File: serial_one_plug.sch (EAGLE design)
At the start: 3 parts

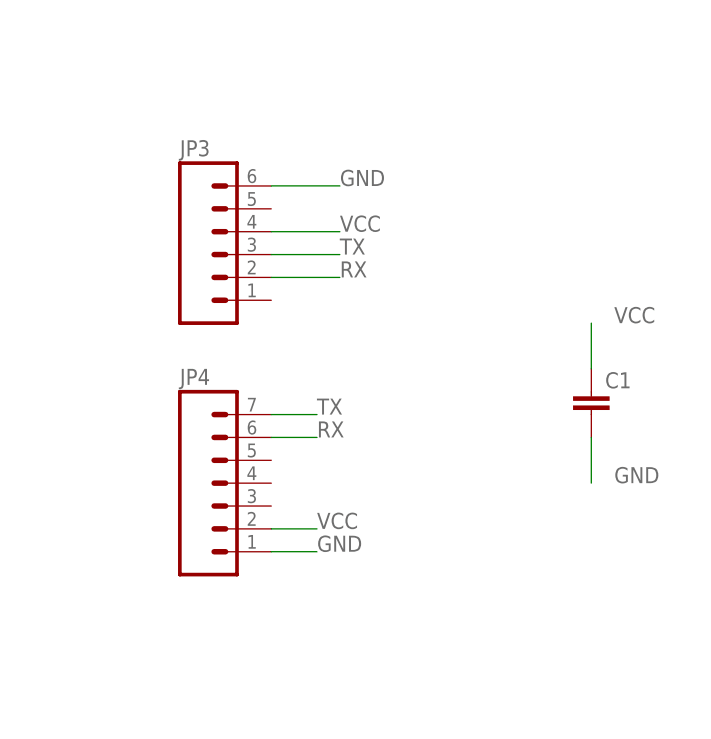
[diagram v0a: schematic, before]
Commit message: serial plug version 2 -- reset + prog
added more (more more!) functionality to the serial plug
has a ground jumper for PD2, pushbutton on reset
enabling it to work with bootloader
printed out, run, it's great.
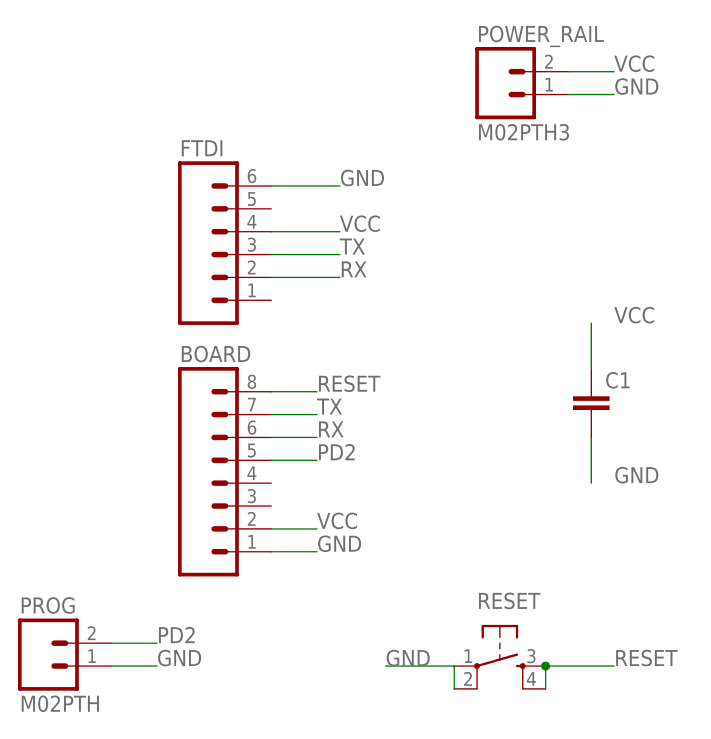
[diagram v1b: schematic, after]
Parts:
- removed JP4: (no value), SparkFun-Connectors:M07LONGPADS
- added BOARD: (no value), SparkFun-Connectors:M08LONGPADS
- added POWER_RAIL: M02PTH3, SparkFun-Connectors:M02PTH3
- added PROG: M02PTH, SparkFun-Connectors:M02PTH
- added RESET: (no value), SparkFun-Electromechanical:TAC_SWITCHPTH
- renumbered JP3 to FTDI
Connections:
- new net PD2: BOARD.5, PROG.2
- new net RESET: BOARD.8, RESET.3, RESET.4
- net GND: now also BOARD.1, POWER_RAIL.1, PROG.1, RESET.1, RESET.2; no longer JP4.1
- net RX: now also BOARD.6; no longer JP4.6
- net TX: now also BOARD.7; no longer JP4.7
- net VCC: now also BOARD.2, POWER_RAIL.2; no longer JP4.2
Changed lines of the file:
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@@
 <parts>
 <part name="C1" library="resistor" deviceset="C-EU" device="C1210"/>
-<part name="JP3" library="SparkFun-Connectors" deviceset="M06" device="LONGPADS"/>
-<part name="JP4" library="SparkFun-Connectors" deviceset="M07" device="LONGPADS"/>
+<part name="FTDI" library="SparkFun-Connectors" deviceset="M06" device="LONGPADS"/>
+<part name="POWER_RAIL" library="SparkFun-Connectors" deviceset="M02" device="PTH3"/>
+<part name="BOARD" library="SparkFun-Connectors" deviceset="M08" device="LONGPADS"/>
+<part name="RESET" library="SparkFun-Electromechanical" deviceset="TAC_SWITCH" device="PTH"/>
+<part name="PROG" library="SparkFun-Connectors" deviceset="M02" device="PTH"/>
 </parts>
 <sheets>
@@
 <instances>
 <instance part="C1" gate="G$1" x="33.02" y="0"/>
-<instance part="JP3" gate="G$1" x="-7.62" y="15.24"/>
-<instance part="JP4" gate="G$1" x="-7.62" y="-12.7"/>
+<instance part="FTDI" gate="G$1" x="-7.62" y="15.24"/>
+<instance part="POWER_RAIL" gate="G$1" x="22.86" y="33.02"/>
+<instance part="BOARD" gate="G$1" x="-7.62" y="-10.16"/>
+<instance part="RESET" gate="S" x="22.86" y="-30.48"/>
+<instance part="PROG" gate="G$1" x="-27.94" y="-30.48"/>
 </instances>
 <busses>
@@
 <wire x1="-2.54" y1="22.86" x2="5.08" y2="22.86" width="0.1524" layer="91"/>
 <label x="5.08" y="22.86" size="1.778" layer="95"/>
-<pinref part="JP3" gate="G$1" pin="6"/>
+<pinref part="FTDI" gate="G$1" pin="6"/>
 </segment>
 <segment>
 <wire x1="-2.54" y1="-17.78" x2="2.54" y2="-17.78" width="0.1524" layer="91"/>
 <label x="2.54" y="-17.78" size="1.778" layer="95"/>
-<pinref part="JP4" gate="G$1" pin="1"/>
+<pinref part="BOARD" gate="G$1" pin="1"/>
 </segment>
 <segment>
@@
 <label x="35.56" y="-10.16" size="1.778" layer="95"/>
 </segment>
+<segment>
+<pinref part="POWER_RAIL" gate="G$1" pin="1"/>
+<wire x1="30.48" y1="33.02" x2="35.56" y2="33.02" width="0.1524" layer="91"/>
+<label x="35.56" y="33.02" size="1.778" layer="95"/>
+</segment>
+<segment>
+<pinref part="RESET" gate="S" pin="1"/>
+<pinref part="RESET" gate="S" pin="2"/>
+<wire x1="10.16" y1="-30.48" x2="17.78" y2="-30.48" width="0.1524" layer="91"/>
+<wire x1="17.78" y1="-30.48" x2="17.78" y2="-33.02" width="0.1524" layer="91"/>
+<label x="10.16" y="-30.48" size="1.778" layer="95"/>
+</segment>
+<segment>
+<pinref part="PROG" gate="G$1" pin="1"/>
+<wire x1="-20.32" y1="-30.48" x2="-15.24" y2="-30.48" width="0.1524" layer="91"/>
+<label x="-15.24" y="-30.48" size="1.778" layer="95"/>
+</segment>
 </net>
 <net name="VCC" class="0">
@@
 <wire x1="-2.54" y1="17.78" x2="5.08" y2="17.78" width="0.1524" layer="91"/>
 <label x="5.08" y="17.78" size="1.778" layer="95"/>
-<pinref part="JP3" gate="G$1" pin="4"/>
+<pinref part="FTDI" gate="G$1" pin="4"/>
 </segment>
 <segment>
 <wire x1="-2.54" y1="-15.24" x2="2.54" y2="-15.24" width="0.1524" layer="91"/>
 <label x="2.54" y="-15.24" size="1.778" layer="95"/>
-<pinref part="JP4" gate="G$1" pin="2"/>
+<pinref part="BOARD" gate="G$1" pin="2"/>
 </segment>
 <segment>
@@
 <label x="35.56" y="7.62" size="1.778" layer="95"/>
 </segment>
+<segment>
+<pinref part="POWER_RAIL" gate="G$1" pin="2"/>
+<wire x1="30.48" y1="35.56" x2="35.56" y2="35.56" width="0.1524" layer="91"/>
+<label x="35.56" y="35.56" size="1.778" layer="95"/>
+</segment>
 </net>
 <net name="TX" class="0">
@@
 <wire x1="-2.54" y1="15.24" x2="5.08" y2="15.24" width="0.1524" layer="91"/>
 <label x="5.08" y="15.24" size="1.778" layer="95"/>
-<pinref part="JP3" gate="G$1" pin="3"/>
+<pinref part="FTDI" gate="G$1" pin="3"/>
 </segment>
 <segment>
 <wire x1="-2.54" y1="-2.54" x2="2.54" y2="-2.54" width="0.1524" layer="91"/>
 <label x="2.54" y="-2.54" size="1.778" layer="95"/>
-<pinref part="JP4" gate="G$1" pin="7"/>
+<pinref part="BOARD" gate="G$1" pin="7"/>
 </segment>
 </net>
@@
 <wire x1="-2.54" y1="12.7" x2="5.08" y2="12.7" width="0.1524" layer="91"/>
 <label x="5.08" y="12.7" size="1.778" layer="95"/>
-<pinref part="JP3" gate="G$1" pin="2"/>
+<pinref part="FTDI" gate="G$1" pin="2"/>
 </segment>
 <segment>
 <wire x1="-2.54" y1="-5.08" x2="2.54" y2="-5.08" width="0.1524" layer="91"/>
 <label x="2.54" y="-5.08" size="1.778" layer="95"/>
-<pinref part="JP4" gate="G$1" pin="6"/>
+<pinref part="BOARD" gate="G$1" pin="6"/>
 </segment>
 </net>
+<net name="RESET" class="0">
+<segment>
+<pinref part="RESET" gate="S" pin="4"/>
+<pinref part="RESET" gate="S" pin="3"/>
+<wire x1="27.94" y1="-33.02" x2="27.94" y2="-30.48" width="0.1524" layer="91"/>
+<wire x1="27.94" y1="-30.48" x2="35.56" y2="-30.48" width="0.1524" layer="91"/>
+<junction x="27.94" y="-30.48"/>
+<label x="35.56" y="-30.48" size="1.778" layer="95"/>
+</segment>
+<segment>
+<pinref part="BOARD" gate="G$1" pin="8"/>
+<wire x1="-2.54" y1="0" x2="2.54" y2="0" width="0.1524" layer="91"/>
+<label x="2.54" y="0" size="1.778" layer="95"/>
+</segment>
+</net>
+<net name="PD2" class="0">
+<segment>
+<pinref part="BOARD" gate="G$1" pin="5"/>
+<wire x1="-2.54" y1="-7.62" x2="2.54" y2="-7.62" width="0.1524" layer="91"/>
+<label x="2.54" y="-7.62" size="1.778" layer="95"/>
+</segment>
+<segment>
+<pinref part="PROG" gate="G$1" pin="2"/>
+<wire x1="-20.32" y1="-27.94" x2="-15.24" y2="-27.94" width="0.1524" layer="91"/>
+<label x="-15.24" y="-27.94" size="1.778" layer="95"/>
+</segment>
+</net>

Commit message: shrunk cap on serial board to 1206 from 1210
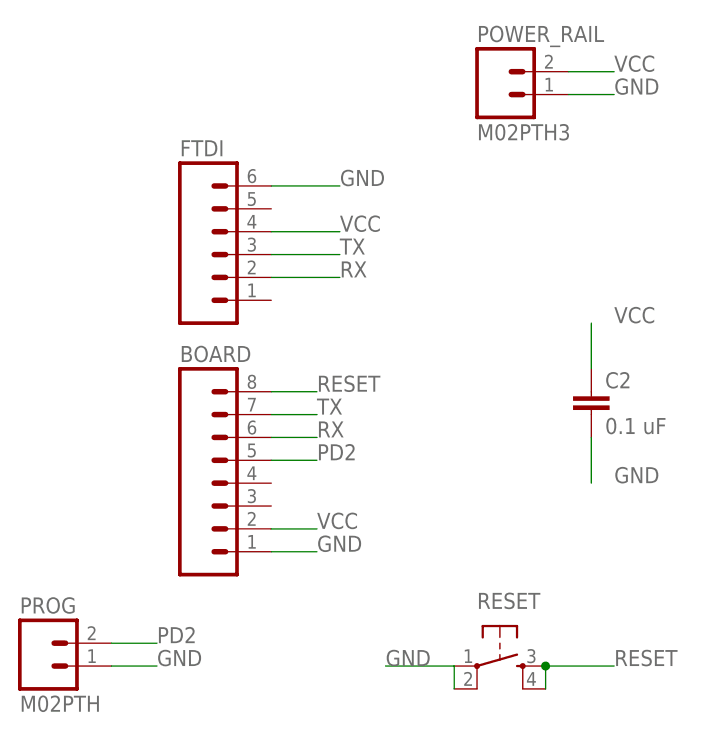
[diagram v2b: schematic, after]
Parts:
- removed C1: (no value), resistor:C-EUC1210
- added C2: 0.1 uF, rcl:C-EUC1206
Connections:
- net GND: now also C2.2; no longer C1.2
- net VCC: now also C2.1; no longer C1.1
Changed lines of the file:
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@@
 </classes>
 <parts>
-<part name="C1" library="resistor" deviceset="C-EU" device="C1210"/>
 <part name="FTDI" library="SparkFun-Connectors" deviceset="M06" device="LONGPADS"/>
 <part name="POWER_RAIL" library="SparkFun-Connectors" deviceset="M02" device="PTH3"/>
@@
 <part name="RESET" library="SparkFun-Electromechanical" deviceset="TAC_SWITCH" device="PTH"/>
 <part name="PROG" library="SparkFun-Connectors" deviceset="M02" device="PTH"/>
+<part name="C2" library="rcl" deviceset="C-EU" device="C1206" value="0.1 uF"/>
 </parts>
 <sheets>
@@
 </plain>
 <instances>
-<instance part="C1" gate="G$1" x="33.02" y="0"/>
 <instance part="FTDI" gate="G$1" x="-7.62" y="15.24"/>
 <instance part="POWER_RAIL" gate="G$1" x="22.86" y="33.02"/>
@@
 <instance part="RESET" gate="S" x="22.86" y="-30.48"/>
 <instance part="PROG" gate="G$1" x="-27.94" y="-30.48"/>
+<instance part="C2" gate="G$1" x="33.02" y="0"/>
 </instances>
 <busses>
@@
 </segment>
 <segment>
-<pinref part="C1" gate="G$1" pin="2"/>
 <wire x1="33.02" y1="-5.08" x2="33.02" y2="-10.16" width="0.1524" layer="91"/>
 <label x="35.56" y="-10.16" size="1.778" layer="95"/>
+<pinref part="C2" gate="G$1" pin="2"/>
 </segment>
 <segment>
@@
 </segment>
 <segment>
-<pinref part="C1" gate="G$1" pin="1"/>
 <wire x1="33.02" y1="2.54" x2="33.02" y2="7.62" width="0.1524" layer="91"/>
 <label x="35.56" y="7.62" size="1.778" layer="95"/>
+<pinref part="C2" gate="G$1" pin="1"/>
 </segment>
 <segment>
